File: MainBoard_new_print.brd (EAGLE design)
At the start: 181 parts, among them T1 BC847, T2 BC847, T3 BC847, U1 STM32F10XRXT6, U2 STM32F10XRXT6, U3 STM32F10XRXT6, Y1 8MHz, Y2 32.768kHz, Y3 8MHz, Y4 32.768kHz, Y5 8MHz, Y6 32.768kHz

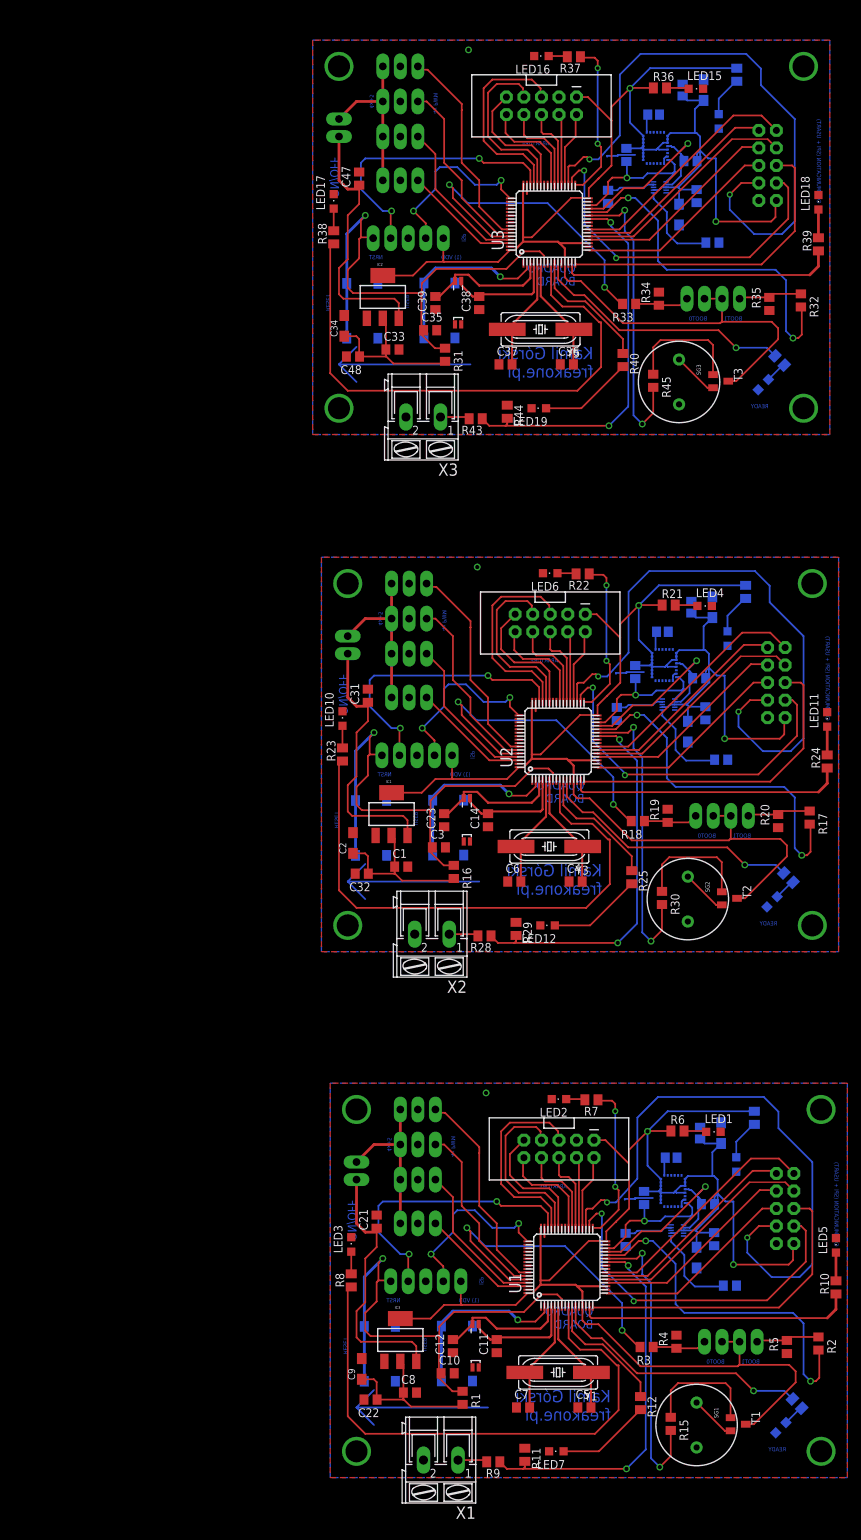
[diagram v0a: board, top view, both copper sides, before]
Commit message: zgubione sygnały przerwań
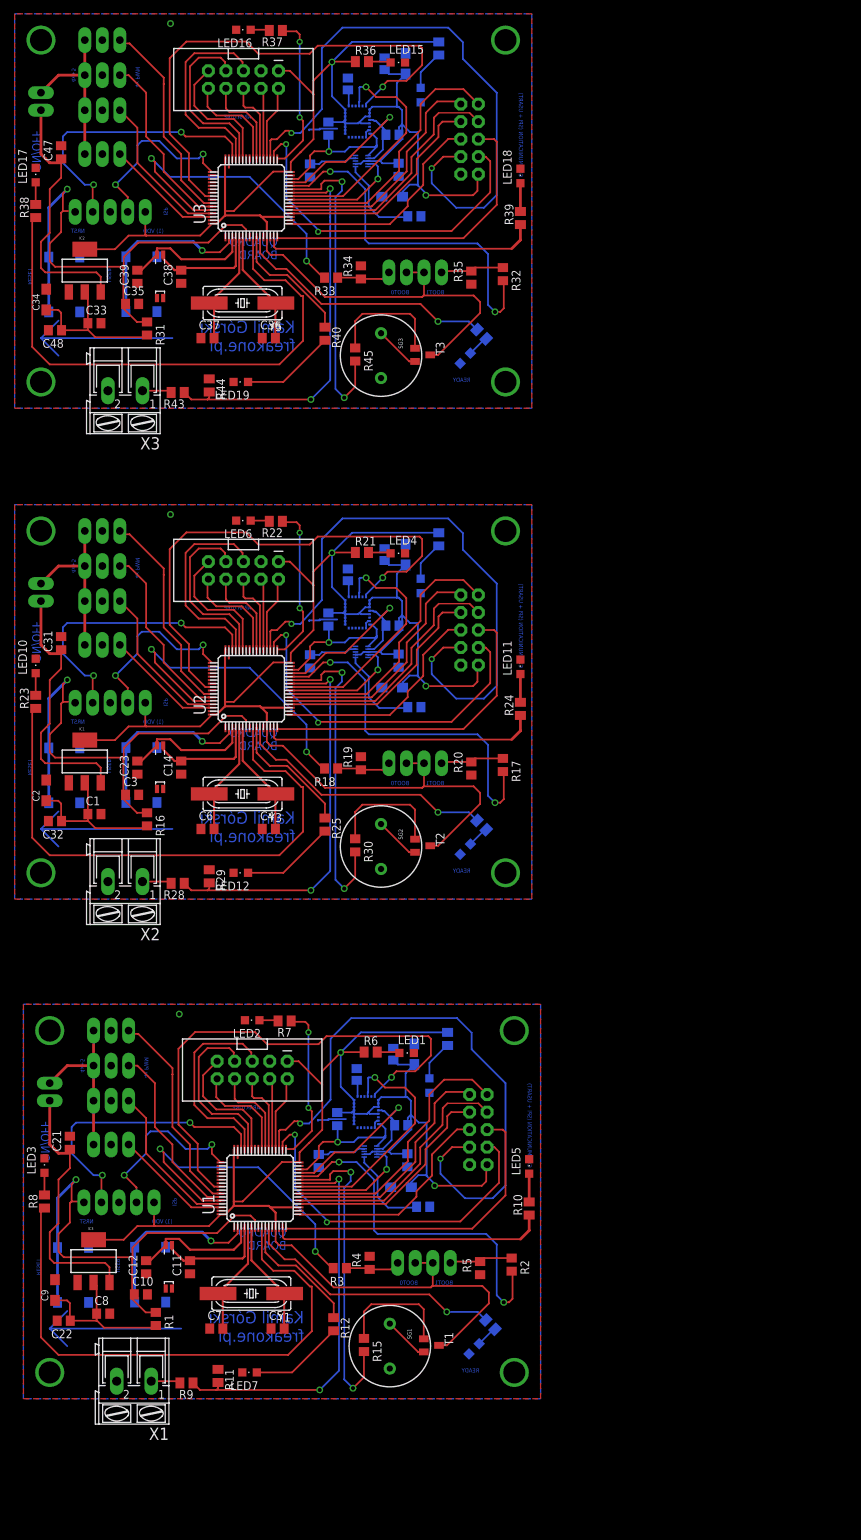
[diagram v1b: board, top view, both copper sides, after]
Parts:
- moved C19 47.1 mm to (38.1, 49.5), turned to 90 degrees
- moved C29 46.3 mm to (36.9, 121.9), turned to 90 degrees
- moved C10 45.9 mm to (6.86, 17.7)
- moved C11 45.9 mm to (14.0, 21.6)
- moved C12 45.9 mm to (7.62, 21.6)
- moved C13 45.9 mm to (47.8, 30.4)
- moved C16 45.9 mm to (45.5, 37.1)
- moved C18 45.9 mm to (43.4, 52.5)
- moved C20 45.9 mm to (46.5, 52.5)
- moved C21 45.9 mm to (-3.43, 39.6)
- moved C5 45.9 mm to (26.7, 12.7)
- moved C8 45.9 mm to (1.40, 14.9)
- moved C9 45.9 mm to (-5.59, 18.3)
- moved IC3 45.9 mm to (0.00, 22.5)
- moved JP1 45.9 mm to (8.76, 31.0)
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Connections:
- net INT_ACC: now also U1.56
- net INT_ACC1: now also U2.56
- net INT_ACC2: now also U3.56
- net INT_GYRO: now also U1.25
- net INT_GYRO1: now also U2.25
- net INT_GYRO2: now also U3.25
- net INT_MAG: now also U1.24
- net INT_MAG1: now also U2.24
- net INT_MAG2: now also U3.24
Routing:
- net INT_ACC: track 0.00 -> 75.4 mm, vias 0 -> 1
- net INT_ACC1: track 0.00 -> 75.4 mm, vias 0 -> 1
- net INT_ACC2: track 0.00 -> 75.4 mm, vias 0 -> 1
- net INT_GYRO2: track 0.00 -> 35.0 mm, vias 0 -> 1
- net INT_GYRO1: track 0.00 -> 35.0 mm, vias 0 -> 1
- net INT_GYRO: track 0.00 -> 35.0 mm, vias 0 -> 1
- net INT_MAG2: track 0.00 -> 17.3 mm, vias 0 -> 1
- net INT_MAG1: track 0.00 -> 17.3 mm, vias 0 -> 1
- net INT_MAG: track 0.00 -> 17.3 mm, vias 0 -> 1
- net MOSI1: track 34.9 -> 38.8 mm
- net MOSI: track 34.9 -> 38.8 mm
- net MOSI2: track 34.9 -> 38.8 mm
- net MISO1: track 31.1 -> 34.5 mm
- net MISO2: track 31.1 -> 34.5 mm
- net MISO: track 31.1 -> 34.5 mm
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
